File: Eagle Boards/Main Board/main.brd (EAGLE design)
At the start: 100 x 100 mm, 83 parts, among them IC1 REG1117, IC2 FT232RL-TUBE, IC3 REG1117, J3 PROG, J4 PROG_RST, U1 TM4C123GH6PMIPM64-L, U10 BSS138SOT-23-3L-L, U11 BSS138SOT-23-3L-L, U12 BSS138SOT-23-3L-L, U13 BSS138SOT-23-3L-L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

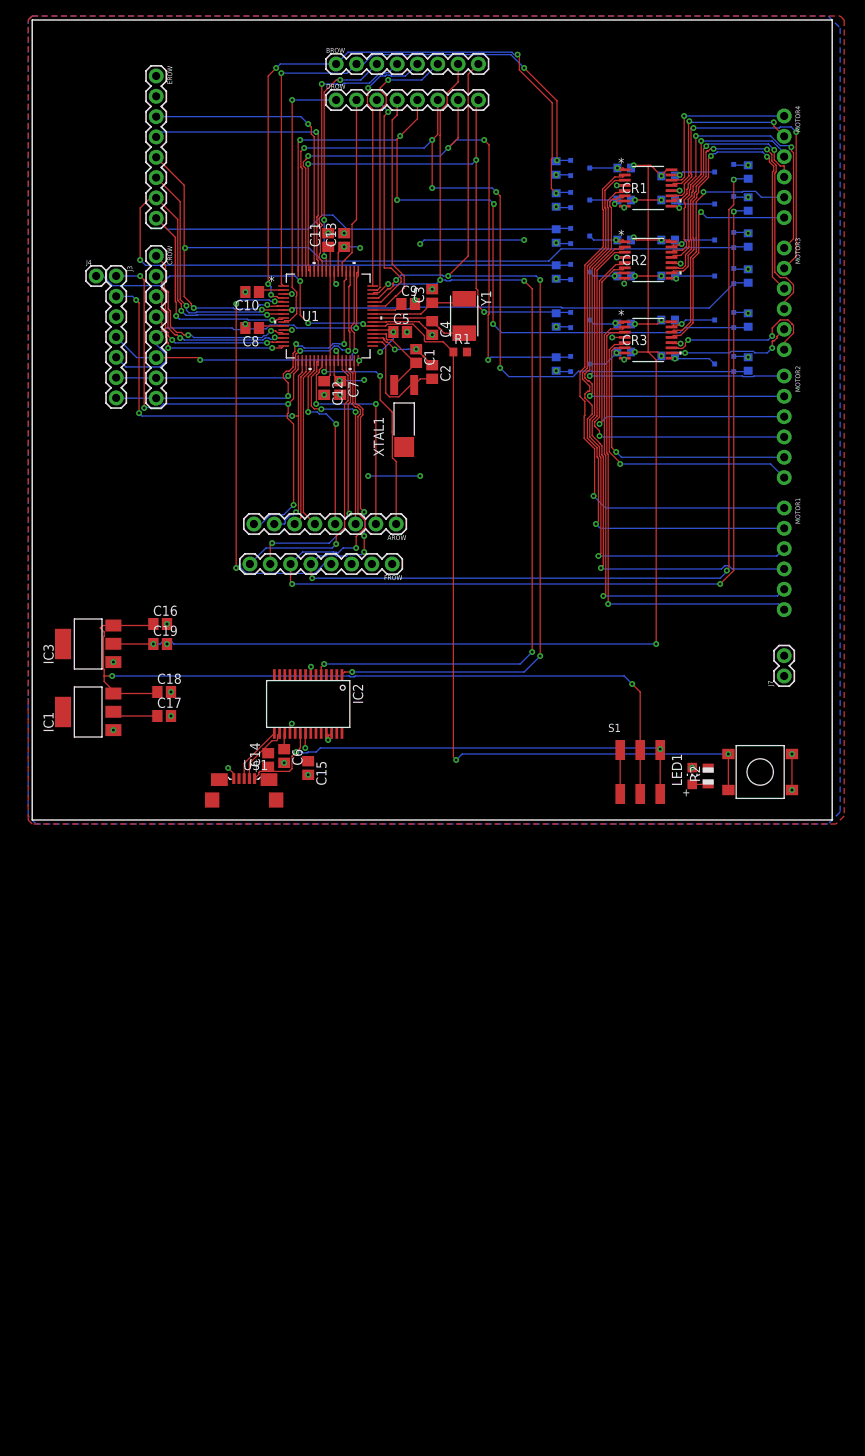
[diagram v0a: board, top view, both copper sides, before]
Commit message: fix a few chips. add RS485 Hookup
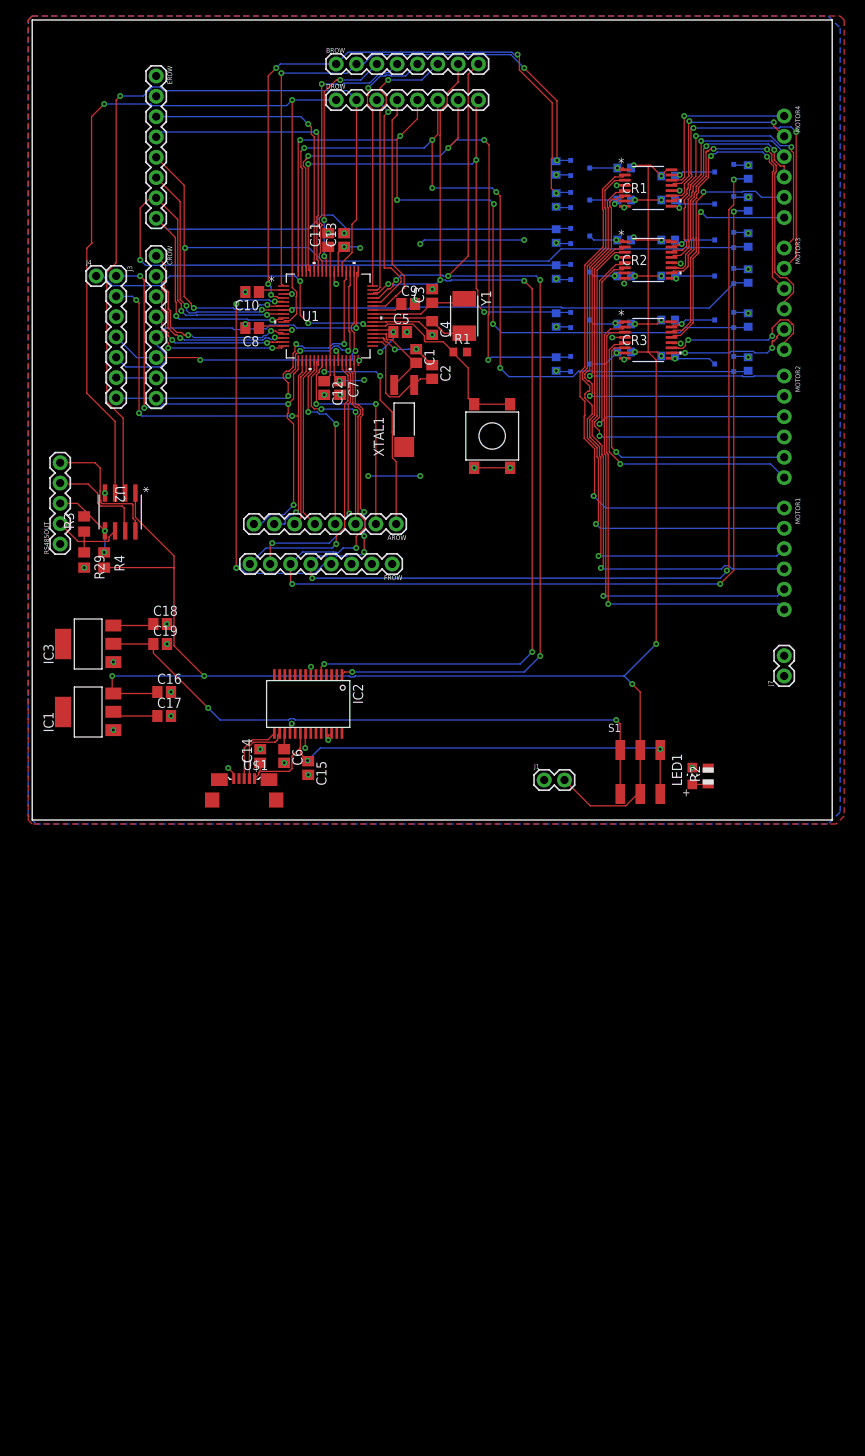
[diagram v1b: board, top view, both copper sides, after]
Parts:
- added J1: (no value), SparkFun-Connectors:1X02
- added R29, R4: 1.2k, resistor:R0805
- added R3: 100, resistor:R0805
- added RS485OUT: (no value), SparkFun-Connectors:1X05
- added U2: SN75LBC179D, tiva:D8
- moved B1 53.7 mm to (57.5, 48.0), turned to 90 degrees
- moved C16 8.51 mm to (16.5, 16.0)
- moved C18 8.51 mm to (16.0, 24.5)
- moved C14 1.12 mm to (28.5, 8.00)
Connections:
- removed net VBUS: C16.1, C18.1, IC1.3, IC3.3, S1.2, S1.5
- new net !RS_RX: RS485OUT.4, U2.7
- new net !RS_TX: R29.1, R3.1, RS485OUT.2, U2.6
- new net 5VIN: C19.1, IC3.2, S1.1, S1.4
- new net RS_RX: RS485OUT.5, U2.8
- new net RS_TX: R3.2, R4.1, RS485OUT.3, U2.5
- net 12V: now also C18.1, IC3.3; no longer S1.1, S1.4
- net 5V: now also C16.1, IC1.3, J1.2, R4.2, S1.2, S1.5, U2.1; no longer C14.1, C15.1, C19.1, IC3.2
- net GND: now also J1.1, R29.2, RS485OUT.1, U2.4
- net U2RX: now also U2.2
- net U2TX: now also U2.3
- net V_USB: now also C14.1, C15.1
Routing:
- net VBUS: track 102.2 -> 0.00 mm, vias 2 -> 0
- net U2RX: track 22.2 -> 104.1 mm, vias 0 -> 1
- net !RST: track 142.6 -> 64.9 mm, vias 5 -> 3
- net 5VIN: track 0.00 -> 77.1 mm, vias 0 -> 2
- net U2TX: track 34.6 -> 109.6 mm, vias 1 -> 2
- net 5V: track 157.2 -> 229.2 mm, vias 14 -> 16
- net RS_RX: track 0.00 -> 17.2 mm
- net !RS_RX: track 0.00 -> 12.9 mm
- net !RS_TX: track 0.00 -> 11.2 mm
- net RS_TX: track 0.00 -> 10.5 mm, vias 0 -> 2
- net V_USB: track 61.7 -> 63.7 mm
- net D-: track 7.55 -> 8.81 mm
- net D+: track 7.23 -> 8.37 mm
- net GND: vias 40 -> 43

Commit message: Update eagle files
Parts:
- renumbered U$1 to USB
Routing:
- net 3.3V: track 77.9 -> 77.2 mm
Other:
- outline, holes or cut-outs redrawn
- board text added: "!DIR"
- board text added: "!EN"
- board text added: "!RST"
- board text added: "!RX"
- board text added: "!Step"
- board text added: "!TX"
- board text added: "3.3V"
- board text added: "5V"
- board text added: "CableBot Main Circuit Board Ver 1.0"
- board text added: "DIR"
- board text added: "EN"
- board text added: "EXT_DBG"
- board text added: "GND"
- board text added: "PA0"
- board text added: "PA1"
- board text added: "PA2"
- board text added: "PA3"
- board text added: "PA4"
- board text added: "PA5"
- board text added: "PA6"
- board text added: "PA7"
- board text added: "PB0"
- board text added: "PB1"
- board text added: "PB2"
- board text added: "PB3"
- board text added: "PB4"
- board text added: "PB5"
- board text added: "PB6"
- board text added: "PB7"
- board text added: "PC0"
- board text added: "PC1"
- board text added: "PC2"
- board text added: "PC3"
- board text added: "PC4"
- board text added: "PC5"
- board text added: "PC6"
- board text added: "PC7"
- board text added: "PD0"
- board text added: "PD1"
- board text added: "PD2"
- board text added: "PD3"
- board text added: "PD4"
- board text added: "PD5"
- board text added: "PD6"
- board text added: "PD7"
- board text added: "PE0"
- board text added: "PE1"
- board text added: "PE2"
- board text added: "PE3"
- board text added: "PE4"
- board text added: "PE5"
- board text added: "PF0"
- board text added: "PF1"
- board text added: "PF2"
- board text added: "PF3"
- board text added: "PF4"
- board text added: "RX"
- board text added: "Step"
- board text added: "TCK"
- board text added: "TDI"
- board text added: "TDO"
- board text added: "TMS"
- board text added: "TX"
- board text added: "U0RX"
- board text added: "U0TX"

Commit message: clean up boards
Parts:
- removed AROW, BROW, CROW, DROW, EROW, FROW: (no value), SparkFun-Connectors:1X08
- removed C18, C19: 1uF, adafruit:C0805
- removed CR2: ST26C31BTR, tiva:TSSOP16
- removed IC3: REG1117, burr-brown:SOT223
- removed R13, R14, R15, R16, R17, R18, R19, R20: 10k, adafruit:R0603
- removed RS485OUT: (no value), SparkFun-Connectors:1X05
- removed U10, U7, U8, U9: BSS138SOT-23-3L-L, tiva:SOT-23-3L-L
- added PROG, RS485: BM05B-ZESS, tiva:BM05B-ZESS
- 3.3V: value REG1117 -> 3.3VREG
- MOTOR1, MOTOR2, MOTOR3, MOTOR4: value (none) -> BM05B-ZESS; device SparkFun-Connectors:1X06_NO_SILK -> tiva:BM05B-ZESS
- moved MOTOR4 187.4 mm to (6.00, -77.5), turned to 0 degrees
- moved MOTOR3 151.2 mm to (6.00, -51.5), turned to 0 degrees
- moved MOTOR2 148.8 mm to (6.00, -64.5), turned to 0 degrees
- moved MOTOR1 117.3 mm to (6.00, -38.5), turned to 0 degrees
- renumbered IC1 to 3.3V
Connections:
- removed net !EN1: CR2.3, MOTOR1.4
- removed net !EN2: CR2.5, MOTOR2.4
- removed net !EN3: CR2.11, MOTOR3.4
- removed net !EN4: CR2.13, MOTOR4.4
- removed net 12V: C18.1, IC3.3
- removed net 5VIN: C19.1, IC3.2, S1.1, S1.4
- removed net EN1: CR2.2, MOTOR1.3
- removed net EN1_SIG: CR2.1, R14.1, U7.3
- removed net EN2: CR2.6, MOTOR2.3
- removed net EN2_SIG: CR2.7, R16.1, U8.3
- removed net EN3: CR2.10, MOTOR3.3
- removed net EN3_SIG: CR2.9, R18.1, U9.3
- removed net EN4: CR2.14, MOTOR4.3
- removed net EN4_SIG: CR2.15, R20.1, U10.3
- removed net M_EN_0: EROW.8, R13.1, U1.9, U7.2
- removed net M_EN_1: EROW.7, R15.1, U1.8, U8.2
- removed net M_EN_2: EROW.6, R17.1, U1.7, U9.2
- removed net M_EN_3: EROW.5, R19.1, U1.6, U10.2
- removed net N$36: FROW.1
- removed net N$37: FROW.2
- removed net N$38: FROW.3
- removed net N$44: EROW.1
- removed net N$45: EROW.2
- removed net PC5: CROW.3, U1.15
- removed net PD4: DROW.4, U1.43
- removed net PF4: FROW.4, U1.5
- new net ENDEFF: U1.43
- new net PB6: U1.1
- new net PB7: U1.4
- new net PE0: U1.9
- new net PE1: U1.8
- new net PE2: U1.7
- new net PE3: U1.6
- net !DIR1: now also MOTOR1.4, MOTOR2.4; no longer MOTOR1.6
- net !DIR2: no longer MOTOR2.6
- net !DIR3: now also MOTOR3.4; no longer MOTOR3.6
- net !DIR4: now also MOTOR4.4; no longer MOTOR4.6
- net !RST: now also B1.4, PROG.5; no longer B1.2
- net !RS_RX: now also RS485.2; no longer RS485OUT.4
- net !RS_TX: now also RS485.4; no longer RS485OUT.2
- net 3.3V: no longer R13.2, R15.2, R17.2, R19.2, U10.1, U7.1, U8.1, U9.1
- net 5V: now also C15.1, IC2.20; no longer CR2.16, R14.2, R16.2, R18.2, R20.2
- net DIR1: now also MOTOR1.3, MOTOR2.3; no longer MOTOR1.5
- net DIR2: no longer MOTOR2.5
- net DIR3: now also MOTOR3.3; no longer MOTOR3.5
- net DIR4: now also MOTOR4.3; no longer MOTOR4.5
- net GND: now also B1.2, MOTOR1.5, MOTOR2.5, MOTOR3.5, MOTOR4.5, RS485.5; no longer B1.4, C18.2, C19.2, CR2.12, CR2.4, CR2.8, IC3.1, RS485OUT.1
- net M_DIR_0: no longer DROW.8
- net M_DIR_1: no longer DROW.7
- net M_DIR_2: no longer DROW.6
- net M_DIR_3: no longer DROW.5
- net PA2: no longer AROW.6
- net PA3: no longer AROW.5
- net PA4: no longer AROW.4
- net PA5: no longer AROW.3
- net PA6: no longer AROW.2
- net PA7: no longer AROW.1
- net PB2: no longer BROW.6
- net PB3: no longer BROW.5
- net PB4: no longer BROW.4
- net PB5: no longer BROW.3
- net PC4: no longer CROW.4
- net PC6: no longer CROW.2
- net PC7: no longer CROW.1
- net PD5: no longer DROW.3
- net PE4: no longer EROW.4
- net PE5: no longer EROW.3
- net PF0: no longer FROW.8
- net PF1: no longer FROW.7
- net RS_RX: now also RS485.1; no longer RS485OUT.5
- net RS_TX: now also RS485.3; no longer RS485OUT.3
- net T0PWM0: now also U1.5; no longer BROW.2, U1.1
- net T0PWM1: now also U1.15; no longer BROW.1, U1.4
- net T1PWM0: no longer FROW.6
- net T1PWM1: no longer FROW.5
- net TCK: now also PROG.1; no longer CROW.8
- net TDI: now also PROG.4; no longer CROW.6
- net TDO: now also PROG.3; no longer CROW.5
- net TMS: now also PROG.2; no longer CROW.7
- net U0RX: now also IC2.1; no longer AROW.8
- net U0TX: now also IC2.5; no longer AROW.7
- net U1RX: now also U2.2; no longer BROW.8, IC2.1
- net U1TX: now also U2.3; no longer BROW.7, IC2.5
- net U2RX: no longer DROW.2, U2.2
- net U2TX: no longer DROW.1, U2.3
- net V_USB: no longer C15.1, IC2.20
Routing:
- net M_EN_3: track 104.3 -> 0.00 mm, vias 3 -> 0
- net U2RX: track 104.1 -> 7.21 mm, vias 1 -> 0
- net M_EN_1: track 91.7 -> 0.00 mm, vias 3 -> 0
- net M_EN_2: track 90.3 -> 0.00 mm, vias 3 -> 0
- net M_EN_0: track 80.9 -> 0.00 mm, vias 2 -> 0
- net 5VIN: track 77.1 -> 0.00 mm, vias 2 -> 0
- net !EN1: track 65.9 -> 0.00 mm, vias 1 -> 0
- net EN1: track 65.3 -> 0.00 mm, vias 1 -> 0
- net PE2: track 0.00 -> 53.5 mm, vias 0 -> 1
- net PF4: track 52.5 -> 0.00 mm, vias 3 -> 0
- net !EN3: track 47.5 -> 0.00 mm, vias 2 -> 0
- net !EN2: track 47.1 -> 0.00 mm, vias 1 -> 0
- net EN2: track 44.9 -> 0.00 mm, vias 1 -> 0
- net EN3: track 42.5 -> 0.00 mm, vias 2 -> 0
- net T0PWM1: track 83.0 -> 42.6 mm, vias 5 -> 2
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
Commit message: new boards
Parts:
- removed U2: SN75LBC179D, tiva:D8
- added H1, H2, H3, H4: MOUNT-HOLE3.2, holes:3,2
- added J2: (no value), SparkFun-Connectors:1X02
- added SN75: SN75LBC179D, tiva:D8
- added U$1: ENDTIVA, tiva:ENDTIVA
- moved MOTOR2 164.1 mm to (98.5, 71.0), turned to 90 degrees
- moved MOTOR1 153.9 mm to (98.5, 84.5), turned to 90 degrees
- moved MOTOR4 152.7 mm to (98.5, 44.0), turned to 90 degrees
- moved MOTOR3 143.0 mm to (98.5, 57.5), turned to 90 degrees
- moved 3.3V 106.5 mm to (75.5, 95.0), turned to 270 degrees
- moved J7 106.1 mm to (21.5, 95.5), turned to 0 degrees
- moved J1 103.6 mm to (13.5, 95.5)
- moved USB 101.7 mm to (61.5, 98.0), turned to 270 degrees
- moved R2 101.3 mm to (38.0, 95.5)
- moved LED1 99.5 mm to (40.0, 95.5)
- moved C17 98.7 mm to (70.0, 96.0), turned to 90 degrees
- moved C15 93.2 mm to (52.0, 98.0), turned to 0 degrees
- moved C16 93.1 mm to (69.5, 92.5), turned to 180 degrees
- moved S1 89.0 mm to (85.0, 94.5), turned to 180 degrees
- moved C14 88.7 mm to (58.5, 91.5), turned to 270 degrees
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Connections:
- removed net EXT_DBG: J3.3
- net !DIR1: no longer MOTOR2.4
- net !DIR2: now also MOTOR2.4
- net !RS_RX: now also SN75.7; no longer U2.7
- net !RS_TX: now also SN75.6; no longer U2.6
- net 3.3V: now also U$1.3.3V
- net 5V: now also J2.1, SN75.1; no longer U2.1
- net DIR1: no longer MOTOR2.3
- net DIR2: now also MOTOR2.3
- net ENDEFF: now also U$1.DIO
- net GND: now also SN75.4, U$1.GND; no longer U2.4
- net RS_RX: now also SN75.8; no longer U2.8
- net RS_TX: now also SN75.5; no longer U2.5
- net U0RX: no longer J3.1
- net U0TX: no longer J3.2
- net U1RX: now also SN75.2; no longer U2.2
- net U1TX: now also SN75.3; no longer U2.3
- net V_USB: now also J2.2
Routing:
- net U2TX: track 95.0 -> 0.00 mm, vias 2 -> 0
- net U1RX: track 121.1 -> 27.1 mm, vias 5 -> 2
- net U1TX: track 119.5 -> 28.1 mm, vias 5 -> 2
- net T1PWM1: track 134.9 -> 47.0 mm, vias 6 -> 1
- net T1PWM0: track 135.0 -> 47.7 mm, vias 4 -> 1
- net M_DIR_2: track 101.3 -> 38.6 mm, vias 5 -> 1
- net M_DIR_3: track 100.5 -> 40.3 mm, vias 5 -> 1
- net M_DIR_1: track 77.7 -> 18.4 mm, vias 4 -> 1
- net PE2: track 53.5 -> 0.00 mm, vias 1 -> 0
- net M4: track 9.43 -> 60.5 mm, vias 1 -> 2
- net U0RX: track 61.9 -> 12.7 mm, vias 4 -> 0
- net DIR2: track 15.6 -> 64.2 mm, vias 1 -> 2
- net M_DIR_0: track 72.3 -> 25.2 mm
- net U0TX: track 58.6 -> 13.9 mm, vias 4 -> 2
- net PE4: track 37.2 -> 0.00 mm, vias 1 -> 0
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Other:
- board size 100 x 100 mm -> 100 x 71 mm
- board text added: "CableBot Control Board V2.0"
- board text added: "LED1"
- board text added: "N/C"
- board text added: "Peripheral Board"
- board text added: "Power Jumper"
- board text added: "RESET"
- board text removed: "!DIR"
- board text removed: "!EN"
- board text removed: "!RST"
- board text removed: "!RX"
- board text removed: "!Step"
- board text removed: "!TX"
- board text removed: "CableBot Main Circuit Board Ver 1.0"
- board text removed: "DIR"
- board text removed: "EN"
- board text removed: "EXT_DBG"
- board text removed: "PA0"
- board text removed: "PA1"
- board text removed: "PA2"
- board text removed: "PA3"
- board text removed: "PA4"
- board text removed: "PA5"
- board text removed: "PA6"
- board text removed: "PA7"
- board text removed: "PB0"
- board text removed: "PB1"
- board text removed: "PB2"
- board text removed: "PB3"
- board text removed: "PB4"
- board text removed: "PB5"
- board text removed: "PB6"
- board text removed: "PB7"
- board text removed: "PC0"
- board text removed: "PC1"
- board text removed: "PC2"
- board text removed: "PC3"
- board text removed: "PC4"
- board text removed: "PC5"
- board text removed: "PC6"
- board text removed: "PC7"
- board text removed: "PD0"
- board text removed: "PD1"
- board text removed: "PD2"
- board text removed: "PD3"
- board text removed: "PD4"
- board text removed: "PD5"
- board text removed: "PD6"
- board text removed: "PD7"
- board text removed: "PE0"
- board text removed: "PE1"
- board text removed: "PE2"
- board text removed: "PE3"
- board text removed: "PE4"
- board text removed: "PE5"
- board text removed: "PF0"
- board text removed: "PF1"
- board text removed: "PF2"
- board text removed: "PF3"
- board text removed: "PF4"
- board text removed: "RX"
- board text removed: "Step"
- board text removed: "TX"
- board text removed: "U0RX"
- board text removed: "U0TX"

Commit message: final board prelim final design
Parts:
- added J5: (no value), SparkFun-Connectors:1X02
- added U$2: BM05B-ZESS, tiva:BM05B-ZESS
- moved J2 7.12 mm to (27.2, 88.8)
- moved LED1 3.75 mm to (43.8, 95.5)
- moved R2 3.75 mm to (41.8, 95.5)
- moved J7 0.75 mm to (20.8, 95.5)
- flipped H3 to the top
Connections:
- new net 3.3VIN: 3.3V.2, C17.1, IC2.17, IC2.4, J5.2, U$2.3
- net 3.3V: now also J5.1, U$2.4; no longer 3.3V.2, C17.1, IC2.17, IC2.4
- net 5V: now also U$2.2
- net GND: now also U$2.5
- net V_USB: now also U$2.1
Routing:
- net 3.3VIN: track 0.00 -> 57.7 mm, vias 0 -> 4
- net 5V: track 210.8 -> 224.1 mm, vias 10 -> 14
- net V_USB: track 64.2 -> 69.4 mm, vias 2 -> 3
- net 3.3V: track 36.8 -> 34.4 mm
- net T1PWM0: track 47.7 -> 46.3 mm
- net GND: vias 41 -> 42
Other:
- outline, holes or cut-outs redrawn
- board text added: "ESTOP"

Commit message: Fix Firmware
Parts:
- PROG: value BM05B-ZESS -> BM08B-ZESS; device tiva:BM05B-ZESS -> tiva:BM08B-ZESS
- moved PROG 2.25 mm to (1.50, 73.2)
- renumbered U$1 to ENDEFFECTOR, U$2 to SWITCH
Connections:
- net !RST: now also PROG.4; no longer PROG.5
- net 5V: now also PROG.2
- net GND: now also PROG.1
- net TCK: now also PROG.8; no longer PROG.1
- net TDI: now also PROG.5; no longer PROG.4
- net TDO: now also PROG.6; no longer PROG.3
- net TMS: now also PROG.7; no longer PROG.2
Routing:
- net TCK: track 44.0 -> 36.7 mm, vias 3 -> 1
- net !RST: track 50.5 -> 45.4 mm
- net TMS: track 40.9 -> 36.8 mm, vias 4 -> 1
- net 5V: track 224.1 -> 225.5 mm
- net TDO: track 34.8 -> 33.7 mm, vias 4 -> 1
- net TDI: track 38.6 -> 38.7 mm, vias 3 -> 2
- net GND: vias 42 -> 43
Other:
- outline, holes or cut-outs redrawn
